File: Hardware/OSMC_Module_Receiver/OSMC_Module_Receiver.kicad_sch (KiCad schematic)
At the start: 5 parts, among them J1 Conn_01x04_Socket, J2 Conn_01x04_Socket, J3 Conn_01x04_Socket, J4 Conn_01x04_Socket, J5 Conn_01x06_Pin

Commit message: update
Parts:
- J5: footprint Connector_PinHeader_2.54mm:PinHeader_1x06_P2.54mm_Horizontal -> Connector_PinHeader_2.54mm:PinHeader_1x06_P2.54mm_Vertical
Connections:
- net Gnd: now reaches J1.1 (Pin_1), J5.1 (Pin_1)
- net Gnd: now also J1.4 (Pin_4)
- net Vdd: now reaches J1.2 (Pin_2), J5.2 (Pin_2)
- net Vdd: now also J1.3 (Pin_3)
- net IO1: now reaches J4.1 (Pin_1), J5.3 (Pin_3)
- net IO2: now reaches J4.2 (Pin_2), J5.4 (Pin_4)
- net I03: now reaches J4.3 (Pin_3), J5.5 (Pin_5)
- net IO4: now reaches J4.4 (Pin_4), J5.6 (Pin_6)
- no-connect marks 0 -> 8
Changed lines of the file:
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@@
 	(generator_version "9.0")
 	(paper "A4")
-	(wire
-		(pts
-			(xy 129.54 83.82) (xy 134.62 83.82)
+	(junction
+		(at 130.81 81.28)
+		(diameter 0)
+		(color 0 0 0 0)
+	)
+	(junction
+		(at 132.08 83.82)
+		(diameter 0)
+		(color 0 0 0 0)
+	)
+	(no_connect
+		(at 167.64 99.06)
+	)
+	(no_connect
+		(at 167.64 86.36)
+	)
+	(no_connect
+		(at 167.64 106.68)
+	)
+	(no_connect
+		(at 167.64 101.6)
+	)
+	(no_connect
+		(at 167.64 93.98)
+	)
+	(no_connect
+		(at 167.64 88.9)
+	)
+	(no_connect
+		(at 167.64 104.14)
+	)
+	(no_connect
+		(at 167.64 91.44)
+	)
+	(wire
+		(pts
+			(xy 129.54 83.82) (xy 132.08 83.82)
+		)
+		(stroke
+			(width 0)
+			(type default)
+		)
+	)
+	(wire
+		(pts
+			(xy 130.81 81.28) (xy 130.81 88.9)
+		)
+		(stroke
+			(width 0)
+			(type default)
+		)
+	)
+	(wire
+		(pts
+			(xy 130.81 81.28) (xy 134.62 81.28)
+		)
+		(stroke
+			(width 0)
+			(type default)
+		)
+	)
+	(wire
+		(pts
+			(xy 132.08 83.82) (xy 134.62 83.82)
 		)
 		(stroke
@@
 	(wire
 		(pts
+			(xy 132.08 83.82) (xy 132.08 86.36)
+		)
+		(stroke
+			(width 0)
+			(type default)
+		)
+	)
+	(wire
+		(pts
+			(xy 132.08 86.36) (xy 134.62 86.36)
+		)
+		(stroke
+			(width 0)
+			(type default)
+		)
+	)
+	(wire
+		(pts
 			(xy 113.03 102.87) (xy 134.62 102.87)
 		)
@@
 	(wire
 		(pts
-			(xy 127 81.28) (xy 134.62 81.28)
+			(xy 127 81.28) (xy 130.81 81.28)
 		)
 		(stroke
@@
 	(wire
 		(pts
+			(xy 130.81 88.9) (xy 134.62 88.9)
+		)
+		(stroke
+			(width 0)
+			(type default)
+		)
+	)
+	(wire
+		(pts
 			(xy 127 92.71) (xy 127 81.28)
 		)
@@
 			(width 0)
 			(type default)
+		)
+	)
+	(label "IO4"
+		(at 123.19 105.41 0)
+		(effects
+			(font
+				(size 1.27 1.27)
+			)
+			(justify left bottom)
+		)
+	)
+	(label "Vdd"
+		(at 123.19 95.25 0)
+		(effects
+			(font
+				(size 1.27 1.27)
+			)
+			(justify left bottom)
+		)
+	)
+	(label "IO1"
+		(at 123.19 97.79 0)
+		(effects
+			(font
+				(size 1.27 1.27)
+			)
+			(justify left bottom)
+		)
+	)
+	(label "IO2"
+		(at 123.19 100.33 0)
+		(effects
+			(font
+				(size 1.27 1.27)
+			)
+			(justify left bottom)
+		)
+	)
+	(label "I03"
+		(at 123.19 102.87 0)
+		(effects
+			(font
+				(size 1.27 1.27)
+			)
+			(justify left bottom)
+		)
+	)
+	(label "Gnd"
+		(at 123.19 92.71 0)
+		(effects
+			(font
+				(size 1.27 1.27)
+			)
+			(justify left bottom)
 		)
 	)
@@
 			)
 		)
-		(property "Footprint" "Connector_PinHeader_2.54mm:PinHeader_1x06_P2.54mm_Horizontal"
+		(property "Footprint" "Connector_PinHeader_2.54mm:PinHeader_1x06_P2.54mm_Vertical"
 			(at 107.95 97.79 0)
 			(effects

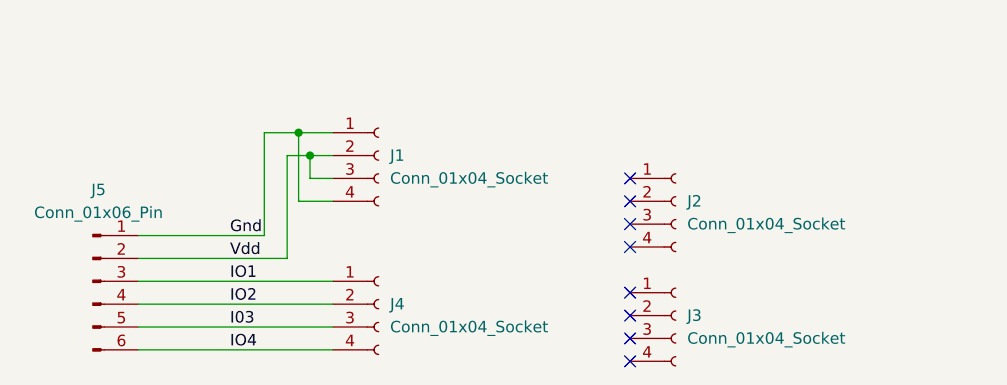
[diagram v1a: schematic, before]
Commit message: added mounting holes
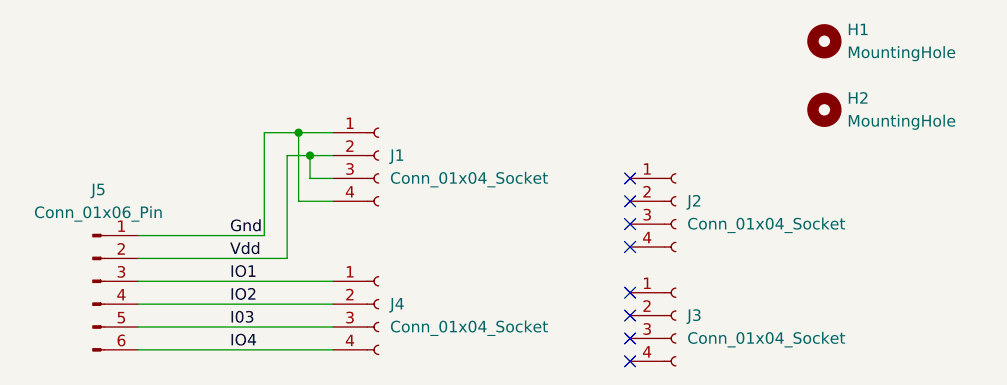
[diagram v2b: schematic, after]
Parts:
- added H1, H2: MountingHole, MountingHole:MountingHole_2.2mm_M2, symbol Mechanical:MountingHole
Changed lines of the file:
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@@
+	)
+	(symbol
+		(lib_id "Mechanical:MountingHole")
+		(at 189.23 71.12 0)
+		(unit 1)
+		(exclude_from_sim no)
+		(in_bom no)
+		(on_board yes)
+		(dnp no)
+		(fields_autoplaced yes)
+		(property "Reference" "H1"
+			(at 191.77 69.8499 0)
+			(effects
+				(font
+					(size 1.27 1.27)
+				)
+				(justify left)
+			)
+		)
+		(property "Value" "MountingHole"
+			(at 191.77 72.3899 0)
+			(effects
+				(font
+					(size 1.27 1.27)
+				)
+				(justify left)
+			)
+		)
+		(property "Footprint" "MountingHole:MountingHole_2.2mm_M2"
+			(at 189.23 71.12 0)
+			(effects
+				(font
+					(size 1.27 1.27)
+				)
+				(hide yes)
+			)
+		)
+		(property "Datasheet" "~"
+			(at 189.23 71.12 0)
+			(effects
+				(font
+					(size 1.27 1.27)
+				)
+				(hide yes)
+			)
+		)
+		(property "Description" "Mounting Hole without connection"
+			(at 189.23 71.12 0)
+			(effects
+				(font
+					(size 1.27 1.27)
+				)
+				(hide yes)
+			)
+		)
+		(instances
+			(project ""
+				(path "/c7166619-b781-4a53-a071-e3ce369183d9"
+					(reference "H1")
+					(unit 1)
+				)
+			)
+		)
 	)
 	(symbol
@@
 					(unit 1)
 				)
+			)
+		)
+	)
+	(symbol
+		(lib_id "Mechanical:MountingHole")
+		(at 189.23 78.74 0)
+		(unit 1)
+		(exclude_from_sim no)
+		(in_bom no)
+		(on_board yes)
+		(dnp no)
+		(fields_autoplaced yes)
+		(property "Reference" "H2"
+			(at 191.77 77.4699 0)
+			(effects
+				(font
+					(size 1.27 1.27)
+				)
+				(justify left)
+			)
+		)
+		(property "Value" "MountingHole"
+			(at 191.77 80.0099 0)
+			(effects
+				(font
+					(size 1.27 1.27)
+				)
+				(justify left)
+			)
+		)
+		(property "Footprint" "MountingHole:MountingHole_2.2mm_M2"
+			(at 189.23 78.74 0)
+			(effects
+				(font
+					(size 1.27 1.27)
+				)
+				(hide yes)
+			)
+		)
+		(property "Datasheet" "~"
+			(at 189.23 78.74 0)
+			(effects
+				(font
+					(size 1.27 1.27)
+				)
+				(hide yes)
+			)
+		)
+		(property "Description" "Mounting Hole without connection"
+			(at 189.23 78.74 0)
+			(effects
+				(font
+					(size 1.27 1.27)
+				)
+				(hide yes)
+			)
+		)
+		(instances
+			(project "OSMC_Module_Receiver"
+				(path "/c7166619-b781-4a53-a071-e3ce369183d9"
+					(reference "H2")
+					(unit 1)
+				)
